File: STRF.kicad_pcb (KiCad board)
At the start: 4 copper layers, 39 x 15 mm, 39 parts, among them J1 USB_B_Micro, J2 SMA, J3 ARM 10pin, U1 XC6206P332MR, U2 USBLC6-2SC6, U3 STM32L432KBU6, U4 nRF24L01P, Y1 16MHz

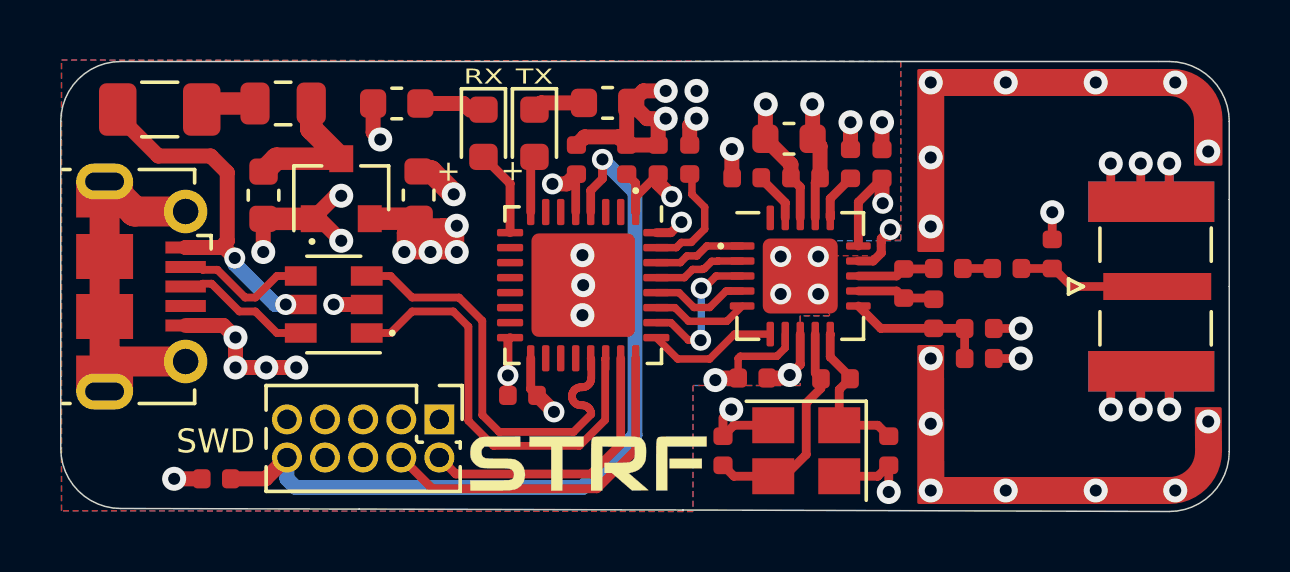
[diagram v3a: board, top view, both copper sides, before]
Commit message: Changed USB connector.
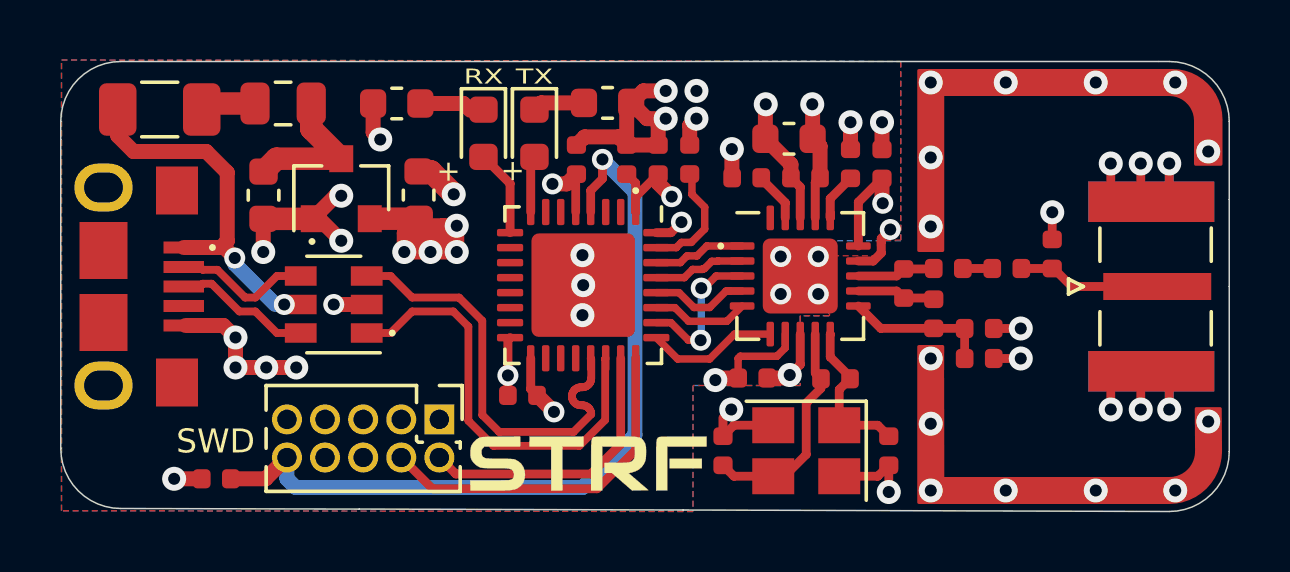
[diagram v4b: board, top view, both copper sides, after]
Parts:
- J1: footprint Connector_USB:USB_Micro-B_Molex-105017-0001 -> 10118193-0001LF:101181930001LF
- R1: value 10k -> 2k2
- moved J1 1.20 mm to (22.8, 34.5)
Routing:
- net Net-(J1-Pad6): track 12.4 -> 0.00 mm
